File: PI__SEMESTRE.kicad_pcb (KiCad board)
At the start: 2 copper layers, 32 parts, among them IC1 LMV358IDR, J1 CX90B-16P1, U1 AMS1117, U11 ESP32-S3-WROOM-1, U14 BME688, U9 GUVA-S12SD

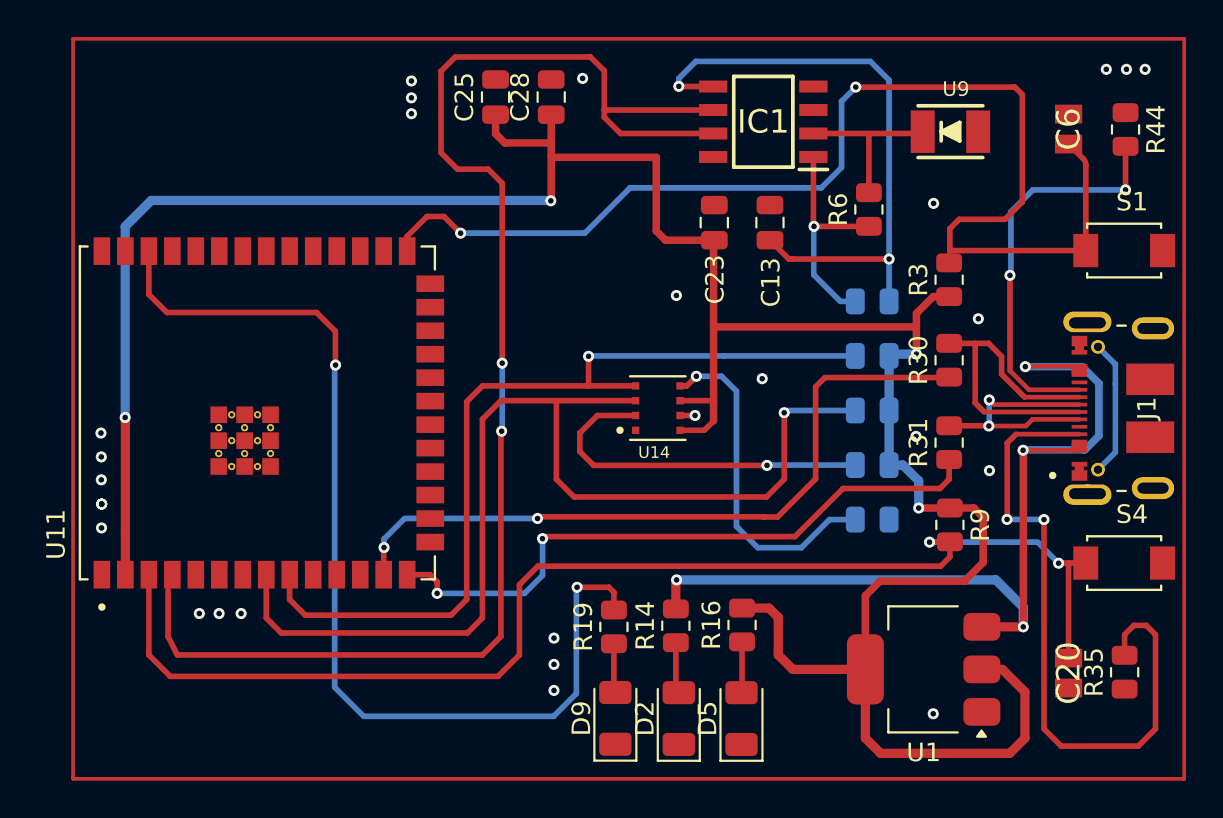
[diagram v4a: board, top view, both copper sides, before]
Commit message: se hicieron los cambios posibles que sugirio el docente, se cambiaron pistas a 45 grados se elimino los valores de los condensadores y resistencias, se hizo tambien el cambio proctecion contra ruido con gnd que nos corrigio el proofesor.
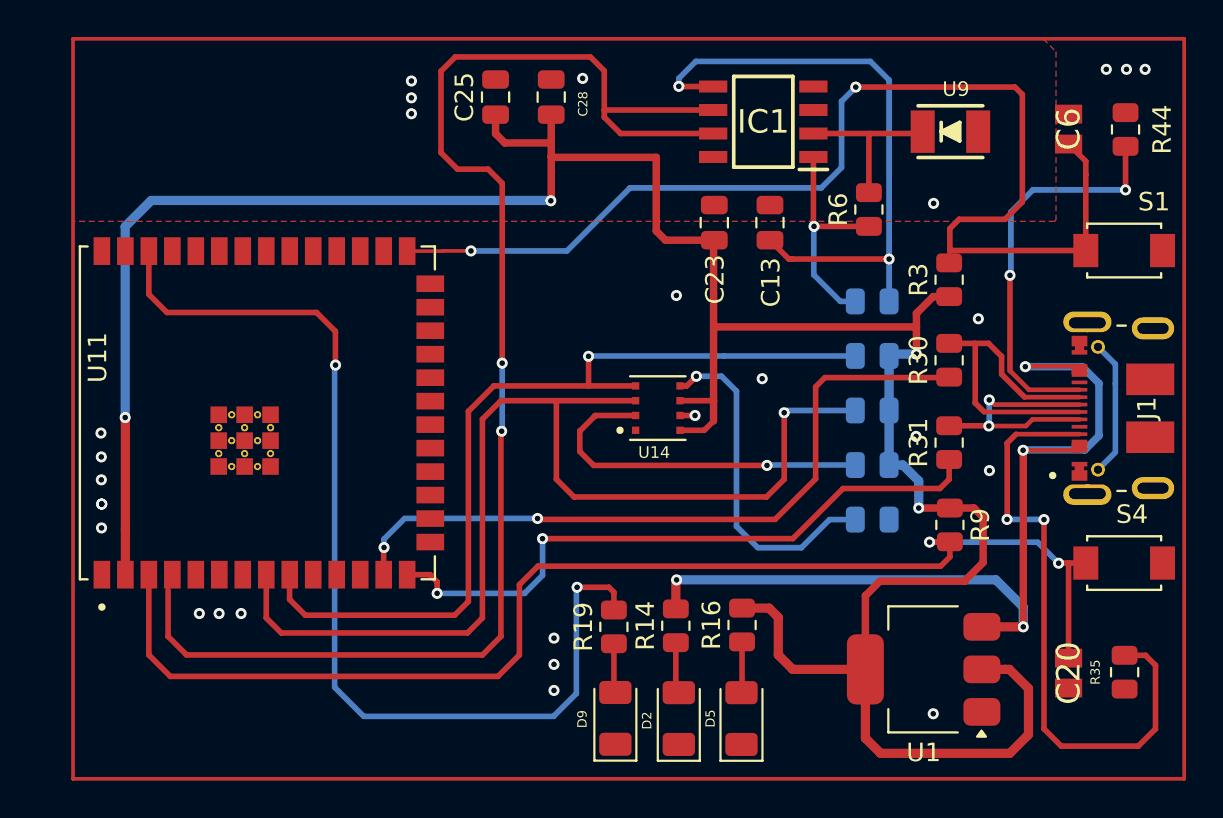
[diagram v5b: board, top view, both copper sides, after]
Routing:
- net Net-(J1-CC1): track 36.7 -> 33.7 mm
- net Boot: track 66.2 -> 64.9 mm

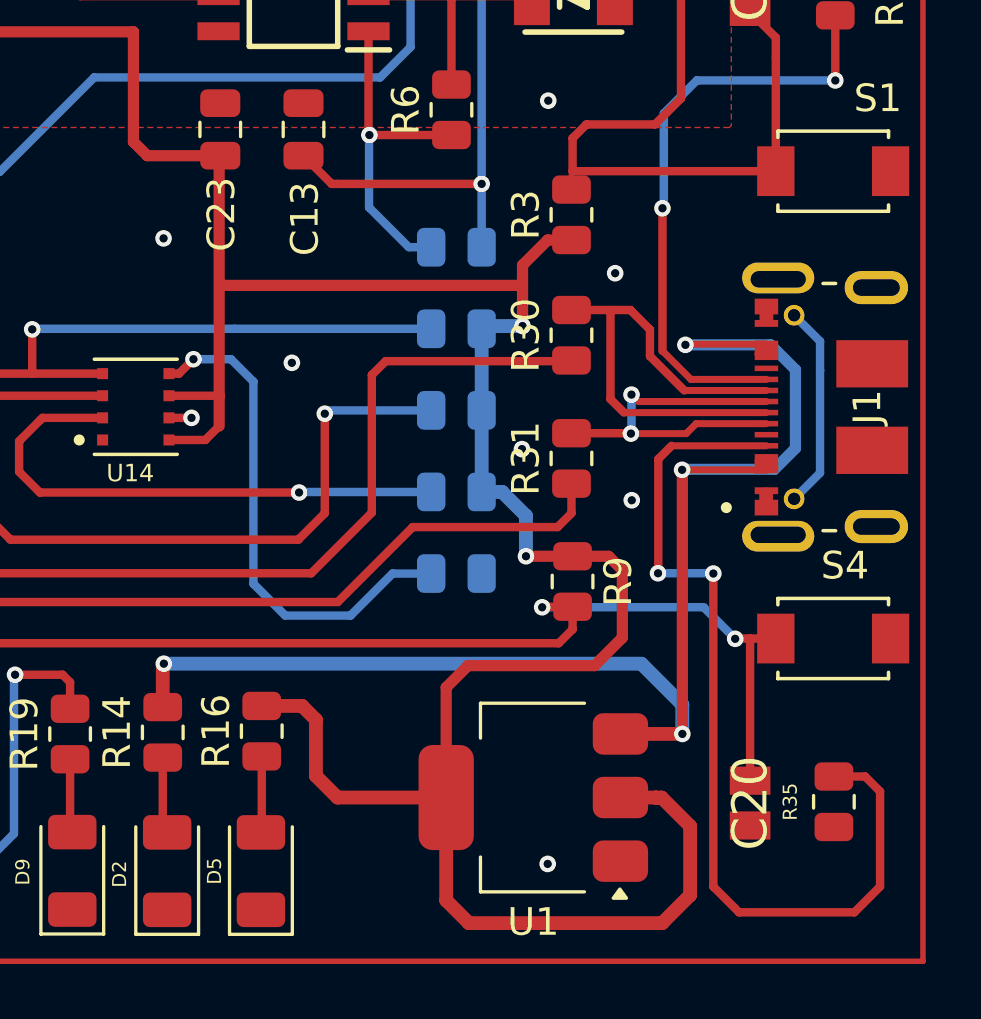
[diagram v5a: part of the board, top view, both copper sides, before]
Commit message: se actualizo la serigrafia en la pcb
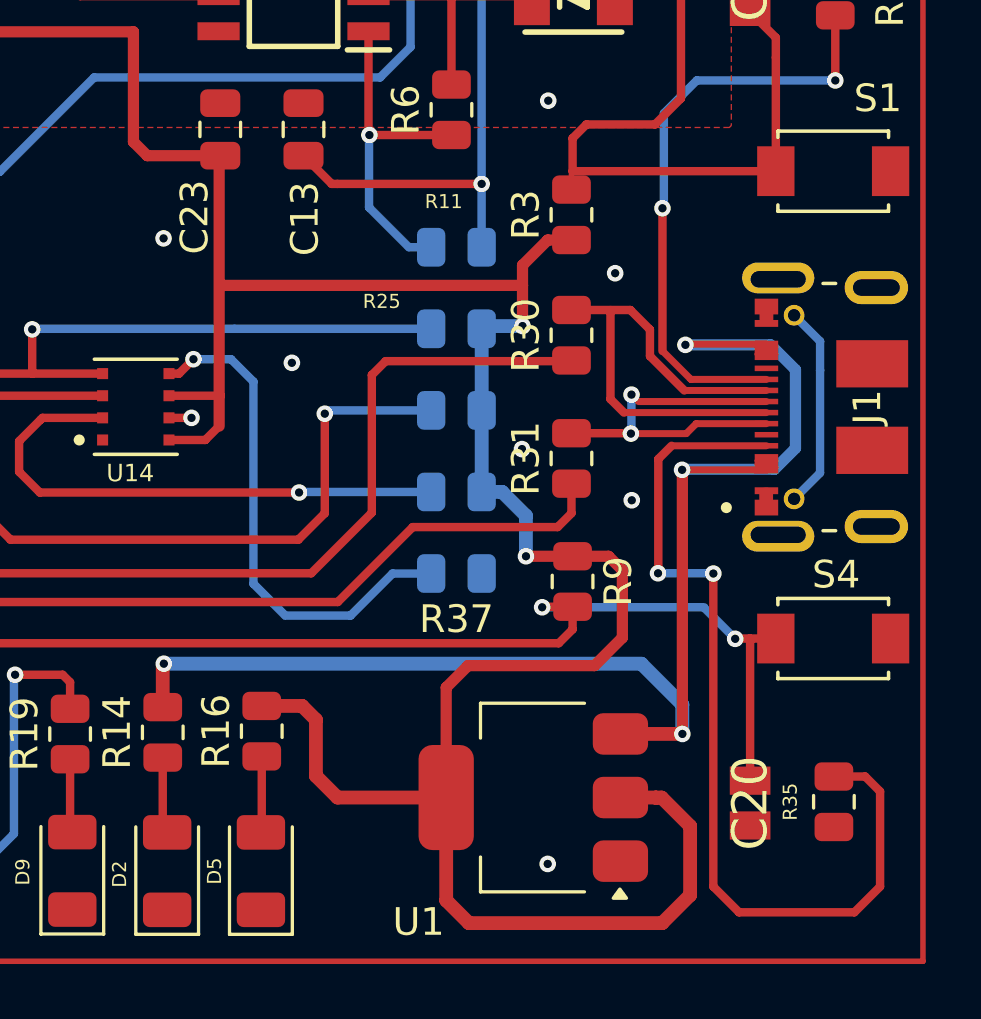
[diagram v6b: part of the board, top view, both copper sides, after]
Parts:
- D2: value LED -> LED 5V
- D5: value LED -> LED 3.3V
- D9: value LED -> LED VIVO
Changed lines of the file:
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@@
 		(tags "capacitor")
 		(property "Reference" "C23"
-			(at 3.07 -0.04 90)
+			(at 3.17 0.93 90)
 			(layer "F.SilkS")
 			(effects
@@
 		(at 125.705 86.53)
 		(property "Reference" "S4"
-			(at 0.425 -2.635 0)
+			(at 0.105 -2.31 0)
 			(layer "F.SilkS")
 			(effects
@@
 			)
 		)
-		(property "Value" "LED"
-			(at -2.72 0.12 180)
+		(property "Value" "LED VIVO"
+			(at -2.81 -0.08 180)
 			(layer "F.Fab")
 			(effects
@@
 		)
 		(property "Value" "BME688"
-			(at 1.7 2.3 0)
+			(at 0.035 3.97 0)
 			(layer "F.Fab")
 			(effects
@@
 			)
 		)
-		(property "Value" "LED"
-			(at -2.77 0.14 180)
+		(property "Value" "LED 5V"
+			(at -2.79 0.01 180)
 			(layer "F.Fab")
 			(effects
@@
 			)
 		)
-		(property "Value" "LED"
-			(at -2.73 0.04 180)
+		(property "Value" "LED 3.3V"
+			(at -2.79 0.22 180)
 			(layer "F.Fab")
 			(effects
@@
 		)
 		(property "Value" "ESP32-S3-WROOM-1"
-			(at 8.03 11.365 90)
+			(at 13.21 0 180)
 			(layer "F.Fab")
 			(effects
@@
 		(tags "CMS SOT")
 		(property "Reference" "U1"
-			(at 0 -4.5 0)
+			(at 4.15 -4.5 0)
 			(layer "F.SilkS")
 			(effects
@@
 		(tags "resistor")
 		(property "Reference" "R37"
-			(at 0 1.65 0)
-			(layer "B.SilkS")
+			(at 0 1.65 -0)
+			(layer "F.SilkS")
 			(effects
 				(font
@@
 					(thickness 0.15)
 				)
-				(justify mirror)
 			)
 		)
@@
 		(tags "resistor")
 		(property "Reference" "R11"
-			(at 0.46 1.65 0)
-			(layer "B.SilkS")
+			(at 0.46 1.65 -0)
+			(layer "F.SilkS")
 			(effects
 				(font
@@
 					(thickness 0.127)
 				)
-				(justify mirror)
 			)
 		)
@@
 		(tags "resistor")
 		(property "Reference" "R25"
-			(at 2.7 0.99 0)
-			(layer "B.SilkS")
+			(at 2.7 0.99 -0)
+			(layer "F.SilkS")
 			(effects
 				(font
@@
 					(thickness 0.127)
 				)
-				(justify mirror)
 			)
 		)
